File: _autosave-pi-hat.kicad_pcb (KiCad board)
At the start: 2 copper layers, 65 x 76 mm, 54 parts, among them J1 Raspberry_Pi_2_3, J2 Conn_SPI, J3 Jack-DC, J4 Conn_01x08, J5 USB_B, J6 Conn_01x02, J7 USB_OUT, J9 Conn_01x02, Q1 Q_NMOS_GDS, Q3 Q_NMOS_GDS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

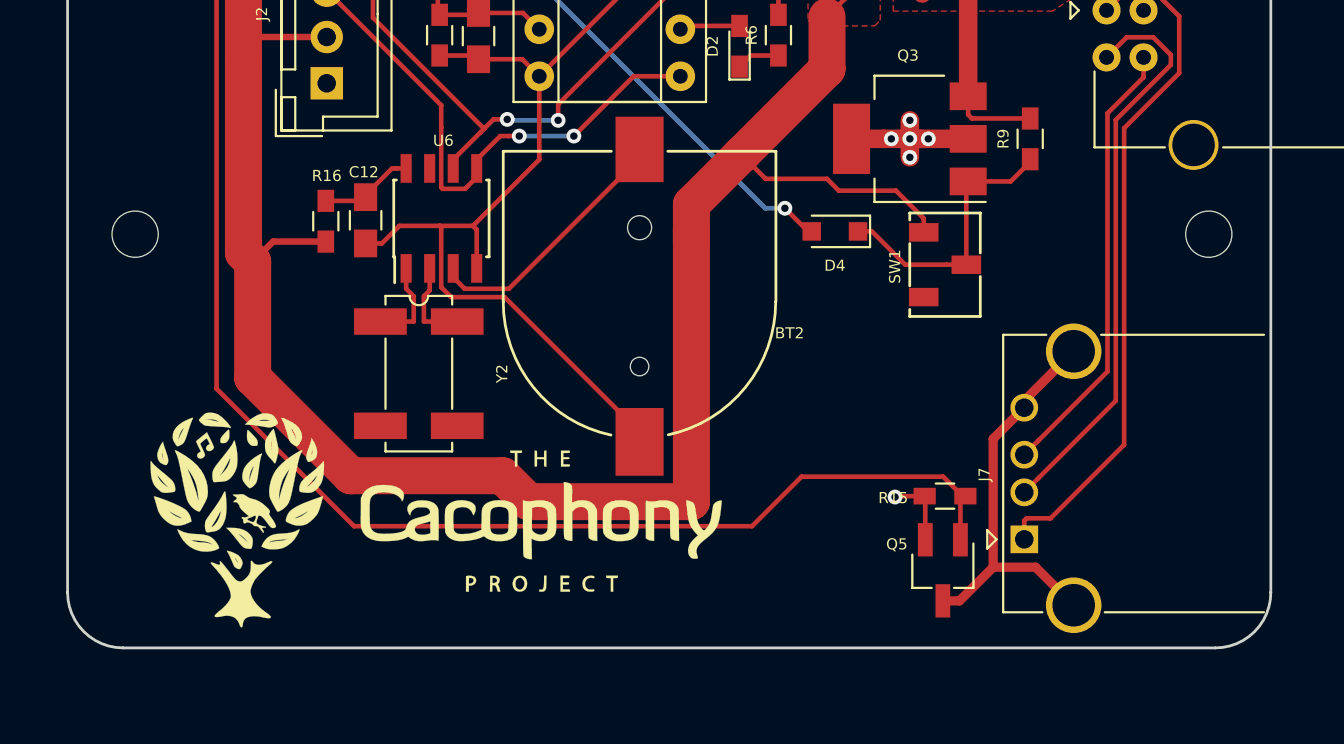
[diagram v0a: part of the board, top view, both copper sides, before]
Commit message: updated pi hat to latest version.
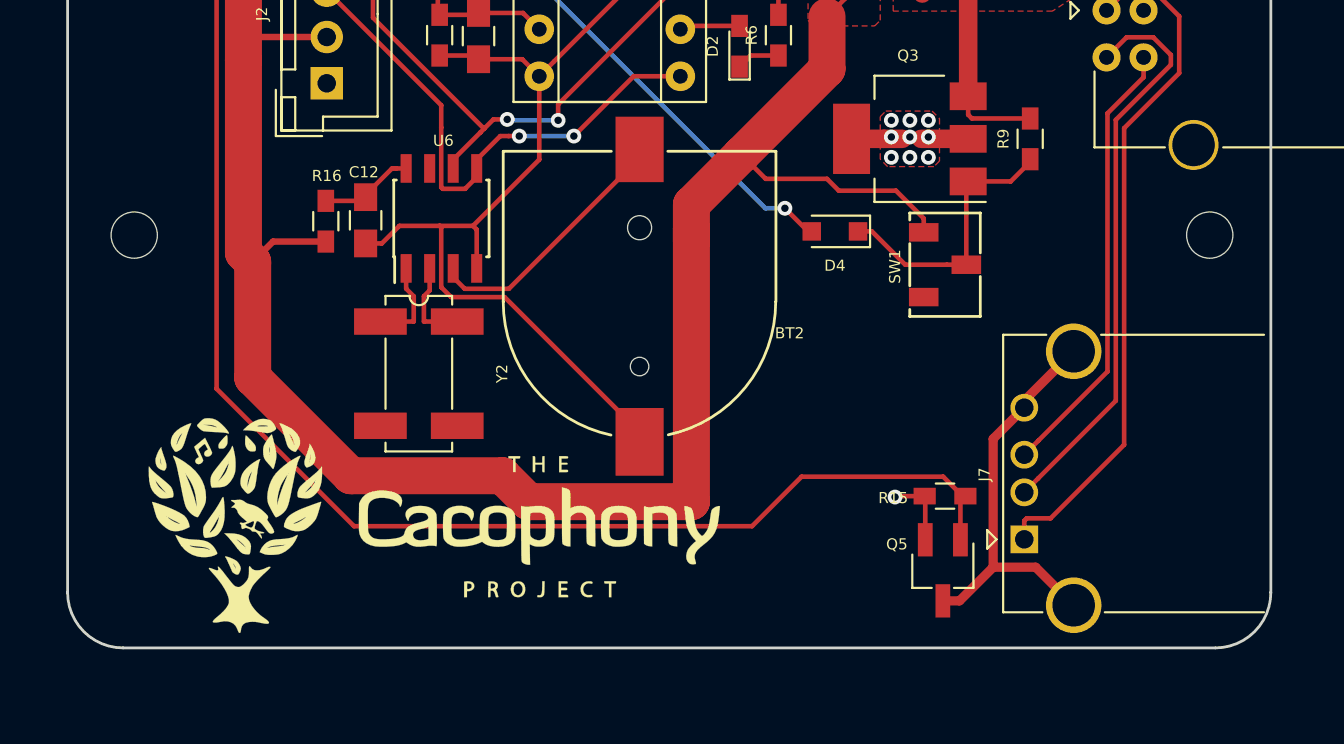
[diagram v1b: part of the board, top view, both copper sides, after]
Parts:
- removed the REF** at (103.7, 152.7)
- removed the REF** at (161.7, 152.7)
- added REF**: MountingHole_2.5mm, Mounting_Holes:MountingHole_2.5mm, F.Cu at (161.7, 152.7)
- added REF**: MountingHole_2.5mm, Mounting_Holes:MountingHole_2.5mm, F.Cu at (103.6, 152.7)
- C4: value 0.1uF -> 100nF
- R18: value 10k -> 10K
- moved G*** 0.32 mm to (119.9, 168.3)
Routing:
- net GND: track 52.3 -> 49.3 mm, vias 11 -> 15
- added copper zone on F.Cu, net GND
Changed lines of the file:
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@@
     (thickness 1.6)
     (drawings 19)
-    (tracks 544)
+    (tracks 545)
     (zones 0)
     (modules 54)
@@
   (page A4)
   (layers
-    (0 F.Cu signal hide)
-    (31 B.Cu signal hide)
+    (0 F.Cu signal)
+    (31 B.Cu signal)
     (32 B.Adhes user)
     (33 F.Adhes user)
@@
       (psa4output false)
       (plotreference true)
-      (plotvalue true)
+      (plotvalue false)
       (plotinvisibletext false)
       (padsonsilk false)
@@
       (drillshape 0)
       (scaleselection 1)
-      (outputdirectory plots/plot1/))
+      (outputdirectory plots/plot2/))
   )
   (net 0 "")
@@
       (effects (font (size 0.6 0.6) (thickness 0.125)))
     )
-    (fp_text value 10k (at 0 1.55 270) (layer F.Fab)
+    (fp_text value 10K (at 0 1.55 270) (layer F.Fab)
       (effects (font (size 0.6 0.6) (thickness 0.125)))
     )
@@
     )
   )
-  (module Mounting_Holes:MountingHole_2.5mm (layer F.Cu)
-    (at 103.65 152.65)
-    (descr "Mounting Hole 2.5mm, no annular")
-    (tags "mounting hole 2.5mm no annular")
-    (fp_text reference REF** (at 0 -3.5) (layer F.SilkS) hide
-      (effects (font (size 0.6 0.6) (thickness 0.125)))
-    )
-    (fp_text value MountingHole_2.5mm (at 0 3.5) (layer F.Fab)
-      (effects (font (size 0.6 0.6) (thickness 0.125)))
-    )
-    (fp_circle (center 0 0) (end 2.75 0) (layer F.CrtYd) (width 0.05))
-    (fp_circle (center 0 0) (end 2.5 0) (layer Cmts.User) (width 0.15))
-    (pad "" np_thru_hole circle (at 0 0) (size 2.5 2.5) (drill 2.5) (layers *.Cu *.Mask)
-      (solder_mask_margin 1.75) (clearance 1.75))
-  )
   (module Capacitors_SMD:C_0805_HandSoldering (layer F.Cu)
     (at 146.7 111.149999 90)
@@
       (effects (font (size 0.6 0.6) (thickness 0.125)))
     )
-    (fp_text value 0.1uF (at 0 1.75 90) (layer F.Fab)
+    (fp_text value 100nF (at 0 1.75 90) (layer F.Fab)
       (effects (font (size 0.6 0.6) (thickness 0.125)))
     )
@@
   )
   (module Mounting_Holes:MountingHole_2.5mm (layer F.Cu)
-    (at 161.65 152.65)
+    (at 161.7 152.7)
+    (descr "Mounting Hole 2.5mm, no annular")
+    (tags "mounting hole 2.5mm no annular")
+    (fp_text reference REF** (at 0 -3.5) (layer F.SilkS) hide
+      (effects (font (size 1 1) (thickness 0.15)))
+    )
+    (fp_text value MountingHole_2.5mm (at 0 3.5) (layer F.Fab)
+      (effects (font (size 1 1) (thickness 0.15)))
+    )
+    (fp_circle (center 0 0) (end 2.75 0) (layer F.CrtYd) (width 0.05))
+    (fp_circle (center 0 0) (end 2.5 0) (layer Cmts.User) (width 0.15))
+    (pad "" np_thru_hole circle (at 0 0) (size 2.5 2.5) (drill 2.5) (layers *.Cu *.Mask)
+      (solder_mask_margin 1.75) (clearance 1.75))
+  )
+  (module Mounting_Holes:MountingHole_2.5mm (layer F.Cu)
+    (at 103.6 152.7)
     (descr "Mounting Hole 2.5mm, no annular")
     (tags "mounting hole 2.5mm no annular")
@@
   )
   (module logo:logo6 (layer F.Cu)
-    (at 120 168)
+    (at 119.9 168.3)
     (fp_text reference G*** (at 0 0) (layer F.SilkS) hide
       (effects (font (size 1.524 1.524) (thickness 0.3)))
@@
   (gr_arc (start 162 172) (end 162 175) (angle -90) (layer Edge.Cuts) (width 0.15))
   (gr_line (start 165 102) (end 165 172) (layer Edge.Cuts) (width 0.15))
+  (via (at 145.5 147.4) (size 0.8) (drill 0.4) (layers F.Cu B.Cu) (net 6))
+  (via (at 146.5 147.4) (size 0.8) (drill 0.4) (layers F.Cu B.Cu) (net 6))
+  (via (at 144.5 147.4) (size 0.8) (drill 0.4) (layers F.Cu B.Cu) (net 6))
   (via (at 113.699999 123.7) (size 0.8) (drill 0.4) (layers F.Cu B.Cu) (net 4))
   (via (at 113.699999 124.6) (size 0.8) (drill 0.4) (layers F.Cu B.Cu) (net 4))
@@
   (segment (start 142.35 147.5) (end 144.1 147.5) (width 1) (layer F.Cu) (net 6))
   (segment (start 144.1 147.5) (end 145.1 147.5) (width 1) (layer F.Cu) (net 6))
-  (via (at 144.5 147.5) (size 0.8) (drill 0.4) (layers F.Cu B.Cu) (net 6))
-  (segment (start 145.1 147.5) (end 146.1 147.5) (width 1) (layer F.Cu) (net 6))
-  (via (at 145.5 147.5) (size 0.8) (drill 0.4) (layers F.Cu B.Cu) (net 6))
-  (segment (start 146.1 147.5) (end 148.65 147.5) (width 1) (layer F.Cu) (net 6))
-  (via (at 146.5 147.5) (size 0.8) (drill 0.4) (layers F.Cu B.Cu) (net 6))
-  (segment (start 145.5 147.5) (end 145.5 146.5) (width 1) (layer F.Cu) (net 6))
-  (segment (start 145.5 146.5) (end 145.5 146.5) (width 1) (layer F.Cu) (net 6))
-  (via (at 145.5 146.5) (size 0.8) (drill 0.4) (layers F.Cu B.Cu) (net 6))
-  (segment (start 145.5 147.5) (end 145.5 148.5) (width 1) (layer F.Cu) (net 6))
-  (via (at 145.5 148.5) (size 0.8) (drill 0.4) (layers F.Cu B.Cu) (net 6))
+  (segment (start 146.1 147.5) (end 146.5 147.5) (width 1) (layer F.Cu) (net 6))
   (segment (start 146.332 166.832) (end 146.3 166.8) (width 0.25) (layer F.Cu) (net 6))
   (segment (start 146.332 169.158) (end 146.332 166.832) (width 0.25) (layer F.Cu) (net 6))
@@
   (segment (start 144.75 166.8) (end 144.7 166.85) (width 0.25) (layer F.Cu) (net 6))
   (segment (start 146.3 166.8) (end 144.75 166.8) (width 0.25) (layer F.Cu) (net 6))
+  (segment (start 146.5 147.5) (end 148.65 147.5) (width 1) (layer F.Cu) (net 6))
+  (via (at 146.5 146.5) (size 0.8) (drill 0.4) (layers F.Cu B.Cu) (net 6))
+  (via (at 144.5 146.5) (size 0.8) (drill 0.4) (layers F.Cu B.Cu) (net 6))
+  (via (at 145.5 146.5) (size 0.8) (drill 0.4) (layers F.Cu B.Cu) (net 6))
+  (via (at 146.5 148.5) (size 0.8) (drill 0.4) (layers F.Cu B.Cu) (net 6))
+  (via (at 145.5 148.5) (size 0.8) (drill 0.4) (layers F.Cu B.Cu) (net 6))
+  (via (at 144.5 148.5) (size 0.8) (drill 0.4) (layers F.Cu B.Cu) (net 6))
   (segment (start 114.6 115.8) (end 117.05 113.35) (width 0.25) (layer F.Cu) (net 18))
   (segment (start 113.95 115.8) (end 114.6 115.8) (width 0.25) (layer F.Cu) (net 18))
@@
       )
     )
+  )
+  (zone (net 6) (net_name GND) (layer F.Cu) (hatch edge 0.508)
+    (connect_pads (clearance 0.2))
+    (min_thickness 0.254)
+    (fill yes (arc_segments 16) (thermal_gap 0.508) (thermal_bridge_width 0.508))
+    (polygon
+      (pts
+        (xy 144.2 146) (xy 146.7 146) (xy 147.1 146.4) (xy 147.1 148.7) (xy 146.8 149)
+        (xy 144.3 149) (xy 143.9 148.6) (xy 143.9 146.3)
+      )
+    )
